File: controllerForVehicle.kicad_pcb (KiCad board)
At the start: 4 copper layers, 99.4 x 99.6 mm, 165 parts, among them IC1 MP2338GTL-Z, J1 Debug, J10 Conn_01x02, J11 Conn_01x02, J12 Conn_01x02, J13 USB_C_Receptacle_PowerOnly_6P, J14 STM_UART, J2 Boot_Sel, J3 VIN, J4 Conn_01x08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

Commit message: 17.45
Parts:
- moved C23 133.2 mm to (23.9, 88.2), turned to -90 degrees
- moved C7 126.9 mm to (-7.85, 141.2), turned to 180 degrees
- moved U7 123.4 mm to (29.0, 83.5), turned to 90 degrees
- moved R27 122.4 mm to (20.1, 155.3), turned to 180 degrees
- moved R44 120.0 mm to (-16.0, 134.4), turned to 180 degrees
- moved R25 119.3 mm to (20.1, 152.9), turned to 180 degrees
- moved C27 116.8 mm to (23.9, 155.3), turned to 180 degrees
- moved R43 116.5 mm to (-16.0, 131.9), turned to 180 degrees
- moved R28 115.6 mm to (19.3, 148.7), turned to 180 degrees
- moved R29 115.4 mm to (17.3, 145.5), turned to -90 degrees
- moved C28 113.5 mm to (23.9, 152.9), turned to 180 degrees
- moved R42 113.0 mm to (-16.0, 129.3), turned to 180 degrees
- moved C24 112.8 mm to (34.1, 88.2), turned to 90 degrees
- moved C25 112.2 mm to (34.7, 82.7), turned to -90 degrees
- moved C33 111.6 mm to (19.6, 145.5), turned to -90 degrees
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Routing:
- net Net-(U11-GPB6): track 97.4 -> 0.00 mm, vias 2 -> 0
- net Net-(U11-GPB7): track 97.2 -> 0.00 mm, vias 2 -> 0
- net Net-(U11-GPB5): track 76.8 -> 0.00 mm, vias 2 -> 0
- net Net-(U11-GPB4): track 75.1 -> 0.00 mm, vias 2 -> 0
- net Net-(U11-GPB3): track 69.1 -> 0.00 mm, vias 2 -> 0
- net Net-(U11-GPB2): track 68.9 -> 0.00 mm, vias 2 -> 0
- net DCEn6: track 52.8 -> 0.00 mm, vias 2 -> 0
- net Net-(U11-GPB1): track 48.6 -> 0.00 mm, vias 2 -> 0
- net DCEn2: track 47.7 -> 0.00 mm, vias 2 -> 0
- net Net-(U11-GPB0): track 47.2 -> 0.00 mm, vias 2 -> 0
- net DCEn1: track 43.4 -> 0.00 mm
- net PCA_7: track 42.0 -> 0.00 mm, vias 2 -> 0
- net PCA_6: track 40.7 -> 0.00 mm, vias 2 -> 0
- net PCA_5: track 38.8 -> 0.00 mm, vias 2 -> 0
- net PCA_4: track 34.9 -> 0.00 mm, vias 2 -> 0
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- removed copper zone on In2.Cu, net 3V3

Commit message: Routing
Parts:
- removed J2: Boot_Sel, Connector_PinHeader_2.54mm:PinHeader_2x03_P2.54mm_Vertical
- removed R71, R73, R74, R75, R76, R78, R79, R80, R81, R82, R83: 100R, Resistor_SMD:R_0805_2012Metric
- added R45: 100R, Resistor_SMD:R_0805_2012Metric, F.Cu at (100.0, 37.3)
- added R46: 100R, Resistor_SMD:R_0805_2012Metric, F.Cu at (97.5, 37.3)
- added R47: 100R, Resistor_SMD:R_0805_2012Metric, F.Cu at (34.5, 37.3)
- added R48: 100R, Resistor_SMD:R_0805_2012Metric, F.Cu at (32.0, 37.3)
- added R49: 100R, Resistor_SMD:R_0805_2012Metric, F.Cu at (61.7, 53.4)
- added R50: 100R, Resistor_SMD:R_0805_2012Metric, F.Cu at (59.1, 53.4)
- added R62: 100R, Resistor_SMD:R_0805_2012Metric, F.Cu at (93.7, 53.4)
- added R63: 100R, Resistor_SMD:R_0805_2012Metric, F.Cu at (91.2, 53.4)
- added R64: 100R, Resistor_SMD:R_0805_2012Metric, F.Cu at (28.2, 53.4)
- R6, R7: value 100K -> 100R
- moved JP1 90.5 mm to (22.0, 79.9), turned to 90 degrees
- moved R51 89.7 mm to (21.7, 76.1), turned to -90 degrees
- moved JP2 85.2 mm to (24.8, 79.9), turned to 90 degrees
- moved R54 84.3 mm to (24.5, 76.1), turned to -90 degrees
- moved JP3 79.9 mm to (27.5, 79.9), turned to 90 degrees
- moved C43 79.0 mm to (31.8, 67.5), turned to -90 degrees
- moved R56 78.9 mm to (27.2, 76.1), turned to -90 degrees
- moved R53 77.6 mm to (33.2, 61.8), turned to 0 degrees
- moved R52 76.8 mm to (33.2, 63.9), turned to 0 degrees
- moved JP4 74.6 mm to (30.3, 79.9), turned to 90 degrees
- moved R57 73.4 mm to (30.0, 76.1), turned to -90 degrees
- moved JP5 69.3 mm to (33.0, 79.9), turned to 90 degrees
- moved C46 68.3 mm to (99.3, 74.7)
- moved C47 68.3 mm to (97.1, 74.7)
- moved JP7 68.3 mm to (110.1, 63.2)
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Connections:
- R6 pad 1: BOOT0 -> Net-(U2-IN1)
- R6 pad 2: Net-(J2-Pad3) -> DCIn3_2
- R7 pad 1: Net-(J2-Pad4) -> Net-(U2-IN2)
- R7 pad 2: BOOT1 -> DCIn3_1
- R70 pad 1: DCIn4_2 -> Net-(U3-IN4)
- R70 pad 2: Net-(U11-GPB0) -> DCIn6_2
- U11 pad 1: Net-(U11-GPB0) -> DCIn6_2
- U11 pad 2: Net-(U11-GPB1) -> DCIn6_1
- U11 pad 21: Net-(U11-GPA0) -> DCIn1_1
- U11 pad 22: Net-(U11-GPA1) -> DCIn1_2
- U11 pad 23: Net-(U11-GPA2) -> DCIn2_1
- U11 pad 24: Net-(U11-GPA3) -> DCIn2_2
- U11 pad 3: Net-(U11-GPB2) -> DCIn5_2
- U11 pad 4: Net-(U11-GPB3) -> DCIn5_1
- U11 pad 5: Net-(U11-GPB4) -> DCIn4_2
- U11 pad 6: Net-(U11-GPB5) -> DCIn4_1
- U11 pad 7: Net-(U11-GPB6) -> DCIn3_2
- U11 pad 8: Net-(U11-GPB7) -> DCIn3_1
- U2 pad 10: DCIn4_1 -> Net-(U2-IN3)
- U2 pad 12: DCIn4_2 -> Net-(U2-IN4)
- U2 pad 5: DCIn3_2 -> Net-(U2-IN1)
- U2 pad 7: DCIn3_1 -> Net-(U2-IN2)
- U3 pad 10: DCIn6_1 -> Net-(U3-IN3)
- U3 pad 12: DCIn6_2 -> Net-(U3-IN4)
- U3 pad 5: DCIn5_1 -> Net-(U3-IN1)
- U3 pad 7: DCIn5_2 -> Net-(U3-IN2)
- U4 pad 10: DCIn2_1 -> Net-(U4-IN3)
- U4 pad 12: DCIn2_2 -> Net-(U4-IN4)
- U4 pad 5: DCIn1_1 -> Net-(U4-IN1)
- U4 pad 7: DCIn1_2 -> Net-(U4-IN2)
- U9 pad 10: PCA_4 -> PCA_3
- U9 pad 11: PCA_5 -> PCA_2
- U9 pad 12: PCA_6 -> PCA_1
- U9 pad 13: PCA_7 -> PCA_0
- U9 pad 6: PCA_0 -> PCA_7
- U9 pad 7: PCA_1 -> PCA_6
- U9 pad 8: PCA_2 -> PCA_5
- U9 pad 9: PCA_3 -> PCA_4
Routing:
- net DCIn5_2: track 2.80 -> 86.9 mm, vias 0 -> 2
- net DCIn5_1: track 2.80 -> 84.2 mm, vias 0 -> 2
- net DCIn6_2: track 6.44 -> 74.4 mm, vias 0 -> 2
- net DCIn6_1: track 6.45 -> 72.5 mm, vias 0 -> 2
- net DCIn3_1: track 2.80 -> 56.4 mm, vias 0 -> 2
- net DCIn3_2: track 2.80 -> 48.9 mm, vias 0 -> 2
- net DCIn1_2: track 2.80 -> 44.9 mm, vias 0 -> 2
- net DCIn4_2: track 6.43 -> 47.4 mm, vias 0 -> 2
- net DCIn1_1: track 2.80 -> 42.1 mm, vias 0 -> 2
- net PCA_0: track 0.00 -> 38.8 mm
- net PCA_1: track 0.00 -> 36.4 mm
- net DCIn4_1: track 6.43 -> 42.2 mm, vias 0 -> 2
- net PCA_2: track 0.00 -> 33.2 mm
- net PCA_3: track 0.00 -> 30.4 mm
- net PCA_4: track 0.00 -> 27.6 mm
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
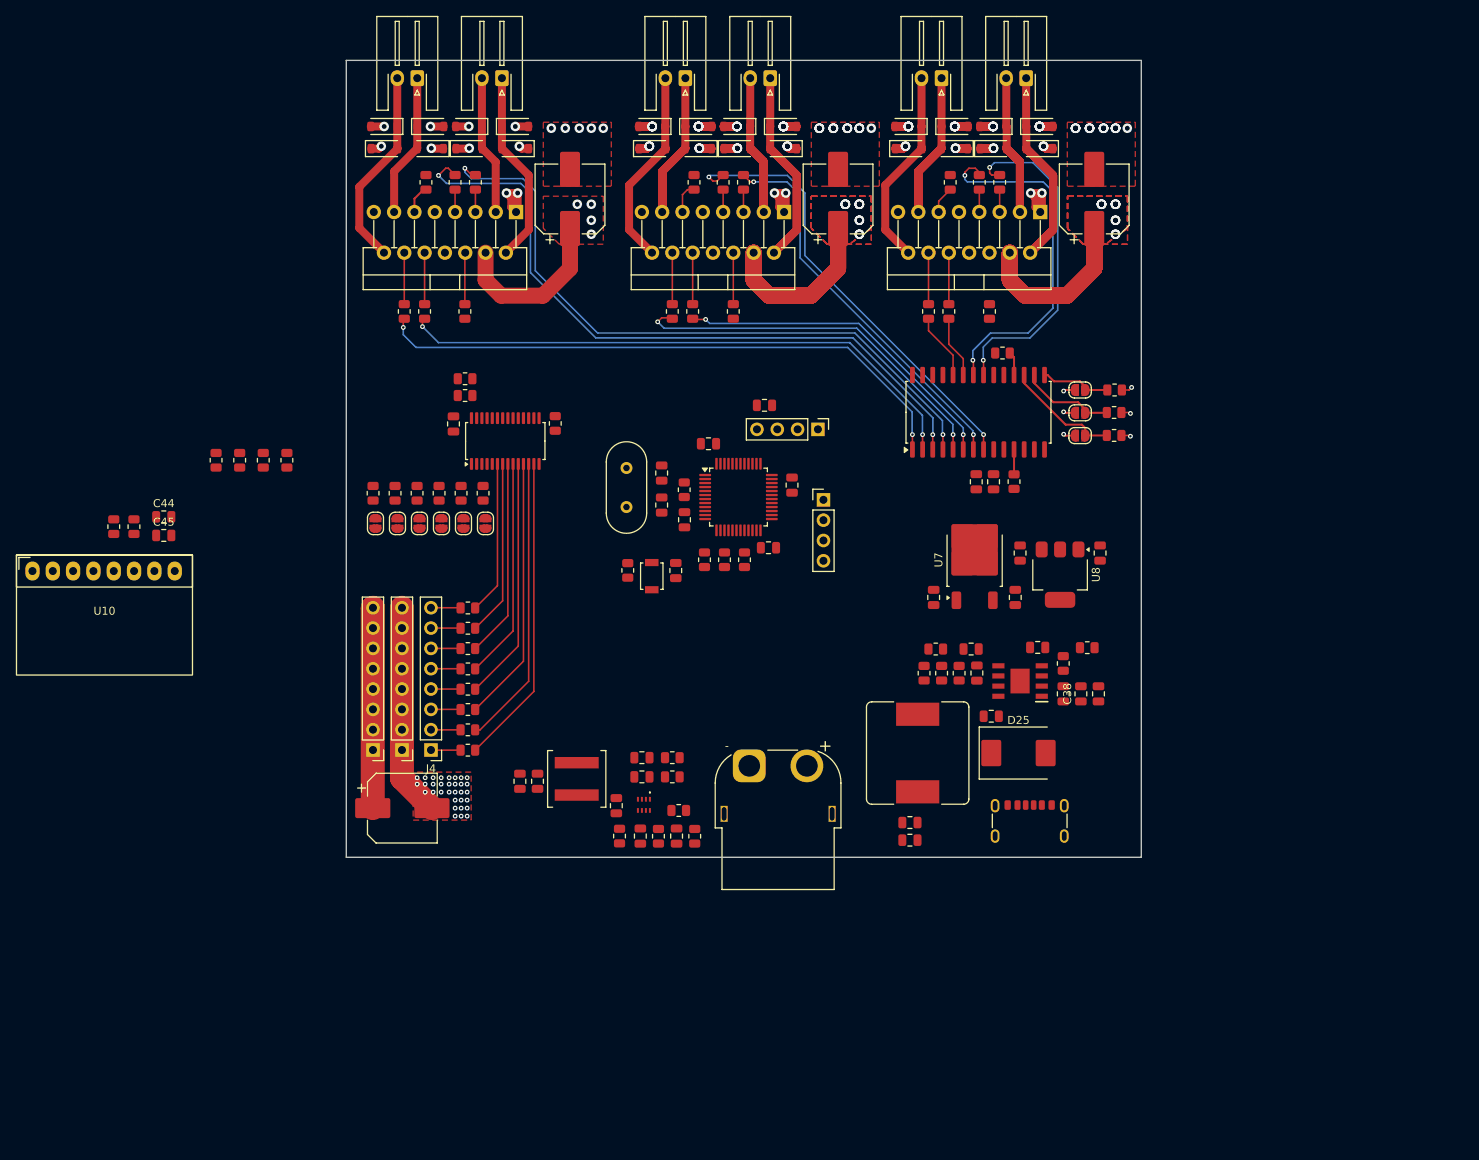
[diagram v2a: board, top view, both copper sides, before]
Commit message: yerleştirme tamamlandı
3d modeller eklenecek
drc kontrolü yapılacak
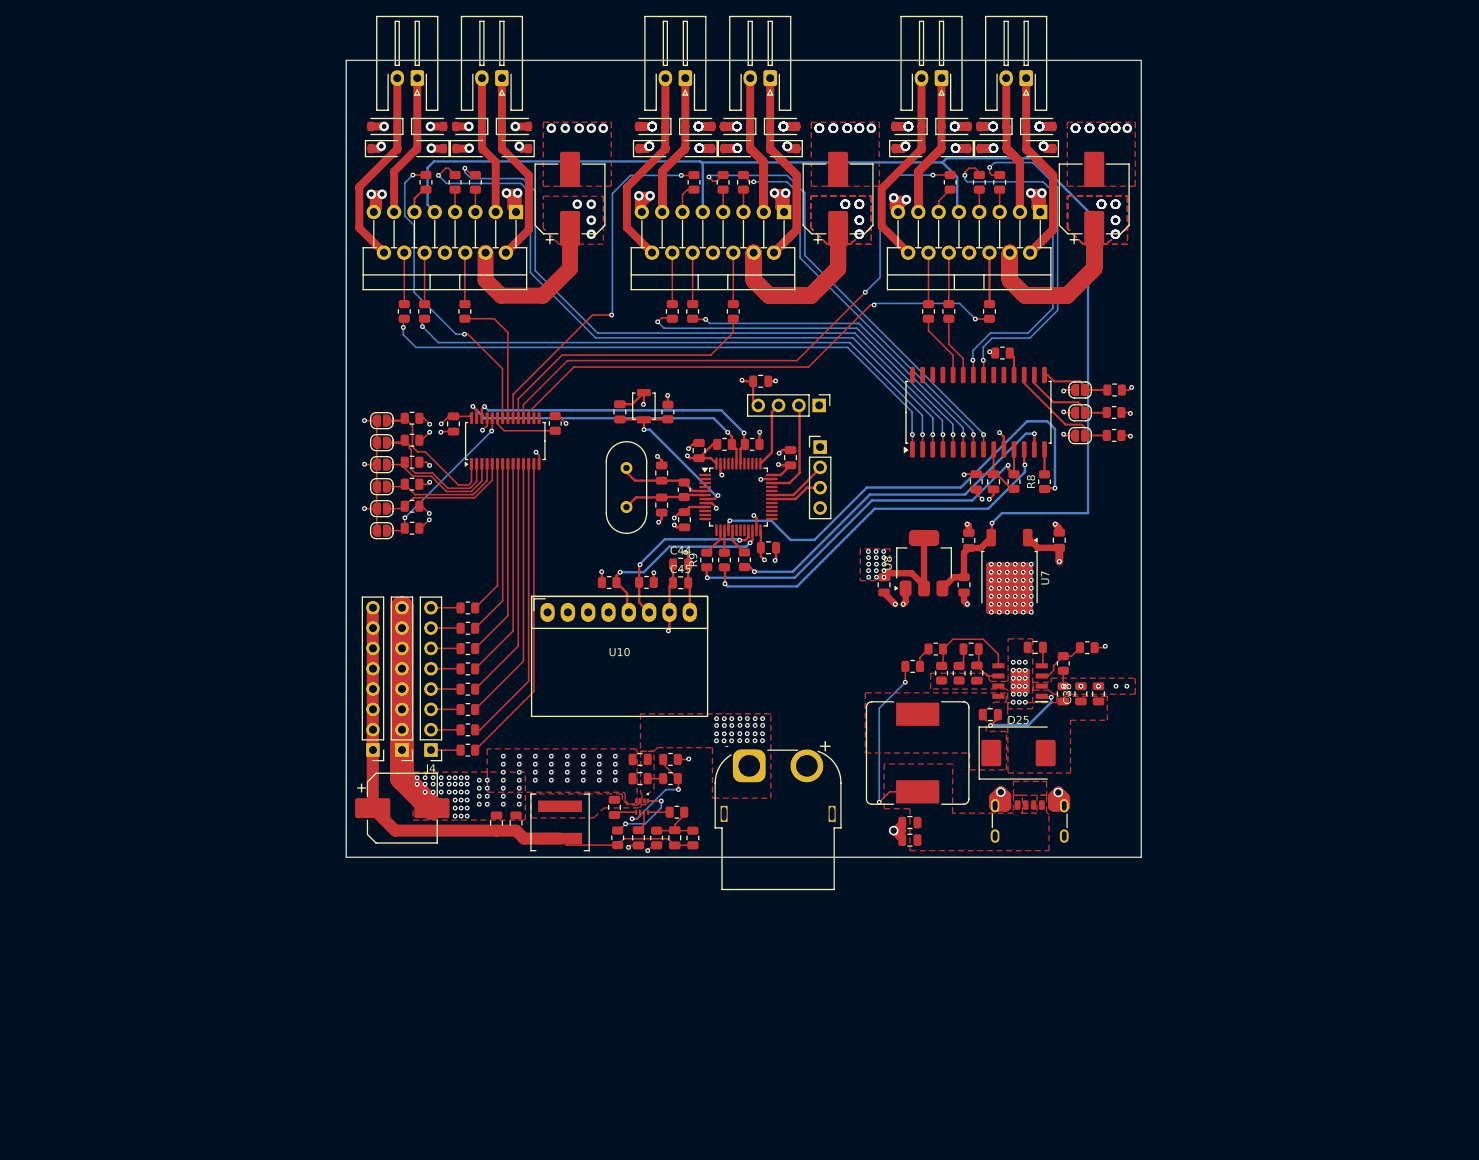
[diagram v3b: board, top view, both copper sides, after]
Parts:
- removed R21, R22: 100R, Resistor_SMD:R_0805_2012Metric
- removed R23, R24: 0R, Resistor_SMD:R_0805_2012Metric
- removed R3: 33R, Resistor_SMD:R_0805_2012Metric
- added R8: 33R, Resistor_SMD:R_0805_2012Metric, F.Cu at (105.7, 74.7)
- added R9: 33R, Resistor_SMD:R_0805_2012Metric, F.Cu at (63.4, 84.5)
- moved C44 64.9 mm to (60.2, 85.0)
- moved C45 64.9 mm to (60.2, 87.3)
- moved U10 64.6 mm to (43.5, 91.0)
- moved R66 64.4 mm to (55.9, 87.3), turned to 0 degrees
- moved R67 62.3 mm to (51.2, 87.3), turned to 0 degrees
- moved R53 36.8 mm to (69.1, 70.0), turned to 180 degrees
- moved R52 33.0 mm to (65.7, 70.0)
- moved C26 27.3 mm to (85.6, 87.6), turned to 90 degrees
- moved SW1 21.3 mm to (55.6, 65.2), turned to -90 degrees
- moved C9 21.0 mm to (52.6, 66.0), turned to -90 degrees
- moved R5 20.4 mm to (58.6, 66.0), turned to -90 degrees
- moved C23 17.3 mm to (107.5, 82.0)
- moved U8 17.1 mm to (90.6, 84.9), turned to 90 degrees
- moved JP6 13.0 mm to (22.8, 80.8), turned to 0 degrees
- moved JP1 12.9 mm to (22.8, 67.0), turned to 0 degrees
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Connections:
- R52 pad 2: PCA_SDA -> I2C1_SDA
- R53 pad 2: PCA_SCL -> I2C1_SCL
- R66 pad 1: MPU_SCL -> I2C2_SCL
- R67 pad 2: MPU_SDA -> I2C2_SDA
- U1 pad 14: SPI1_CS -> Net-(U1-PA4)
- U1 pad 16: Net-(U1-PA6) -> SPI1_MISO
- U10 pad 5: MPU_SDA -> I2C2_SDA
- U10 pad 6: MPU_SCL -> I2C2_SCL
- U11 pad 14: SPI1_MISO -> Net-(U11-SO)
- U9 pad 26: PCA_SCL -> I2C1_SCL
- U9 pad 27: PCA_SDA -> I2C1_SDA
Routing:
- net 5V1: track 0.00 -> 167.8 mm, vias 0 -> 1
- net GND: track 136.6 -> 237.0 mm, vias 132 -> 282
- net 3V3: track 4.40 -> 87.9 mm, vias 3 -> 34
- net DCEn2: track 0.00 -> 73.3 mm, vias 0 -> 2
- net DCEn1: track 0.00 -> 64.8 mm, vias 0 -> 2
- net SPI1_MISO: track 0.00 -> 58.2 mm, vias 0 -> 2
- net SPI1_SCK: track 0.00 -> 48.5 mm, vias 0 -> 2
- net SPI1_CS: track 3.11 -> 49.3 mm, vias 0 -> 2
- net DCEn4: track 0.00 -> 45.8 mm, vias 0 -> 2
- net SPI1_MOSI: track 0.00 -> 45.6 mm, vias 0 -> 2
- net 5V2: track 25.1 -> 67.7 mm
- net I2C1_SCL: track 0.00 -> 39.5 mm, vias 0 -> 2
- net I2C1_SDA: track 0.00 -> 39.2 mm, vias 0 -> 2
- net DCEn6: track 0.00 -> 38.4 mm, vias 0 -> 2
- net DCEn3: track 0.00 -> 34.5 mm
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- added copper zone on F.Cu, net 3V3
- added copper zone on In2.Cu, net 3V3
- added copper zone on F.Cu, net 5VRPi
- added copper zone on F.Cu, net Net-(D25-K)
- added copper zone on F.Cu, net Net-(IC1-SW)
